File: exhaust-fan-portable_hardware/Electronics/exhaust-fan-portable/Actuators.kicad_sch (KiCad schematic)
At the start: 20 parts, among them Q1 NMOS, Q2 NMOS, Q3 NMOS, U3 LMV321, U6 LMV321, U7 LMV321

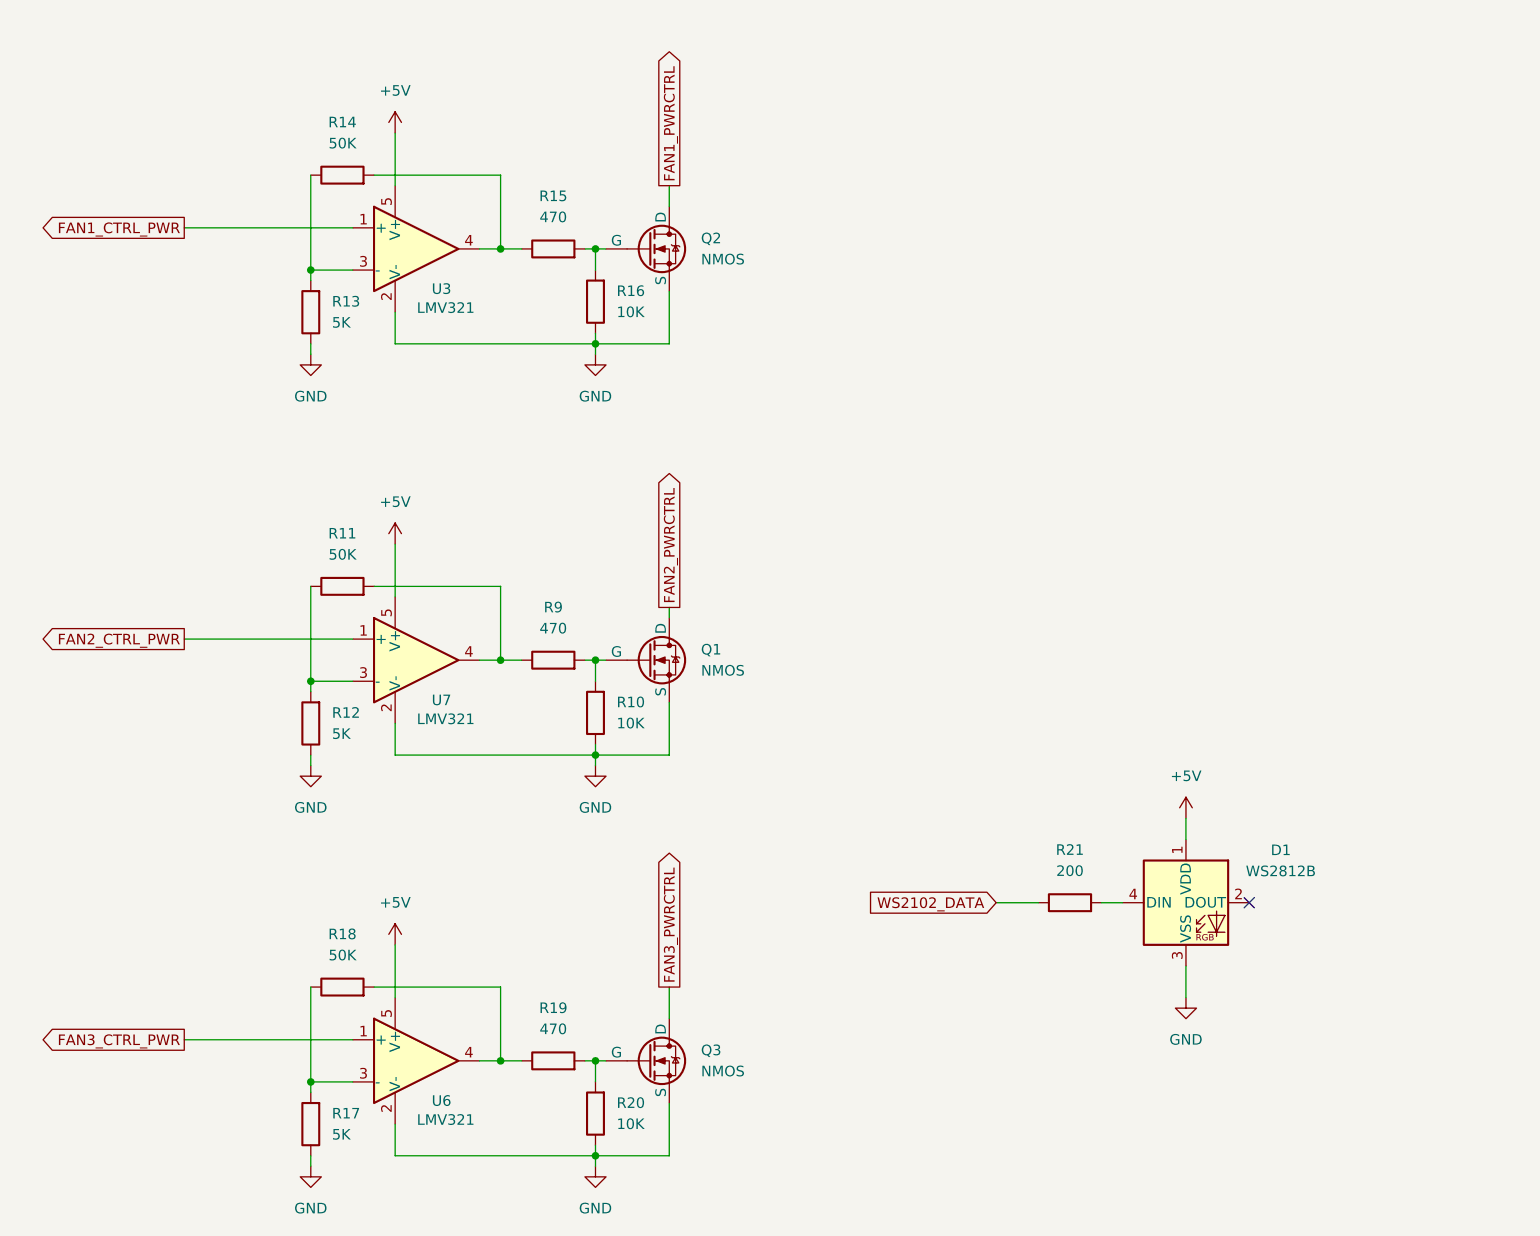
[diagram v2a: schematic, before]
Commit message: updated mechanical information
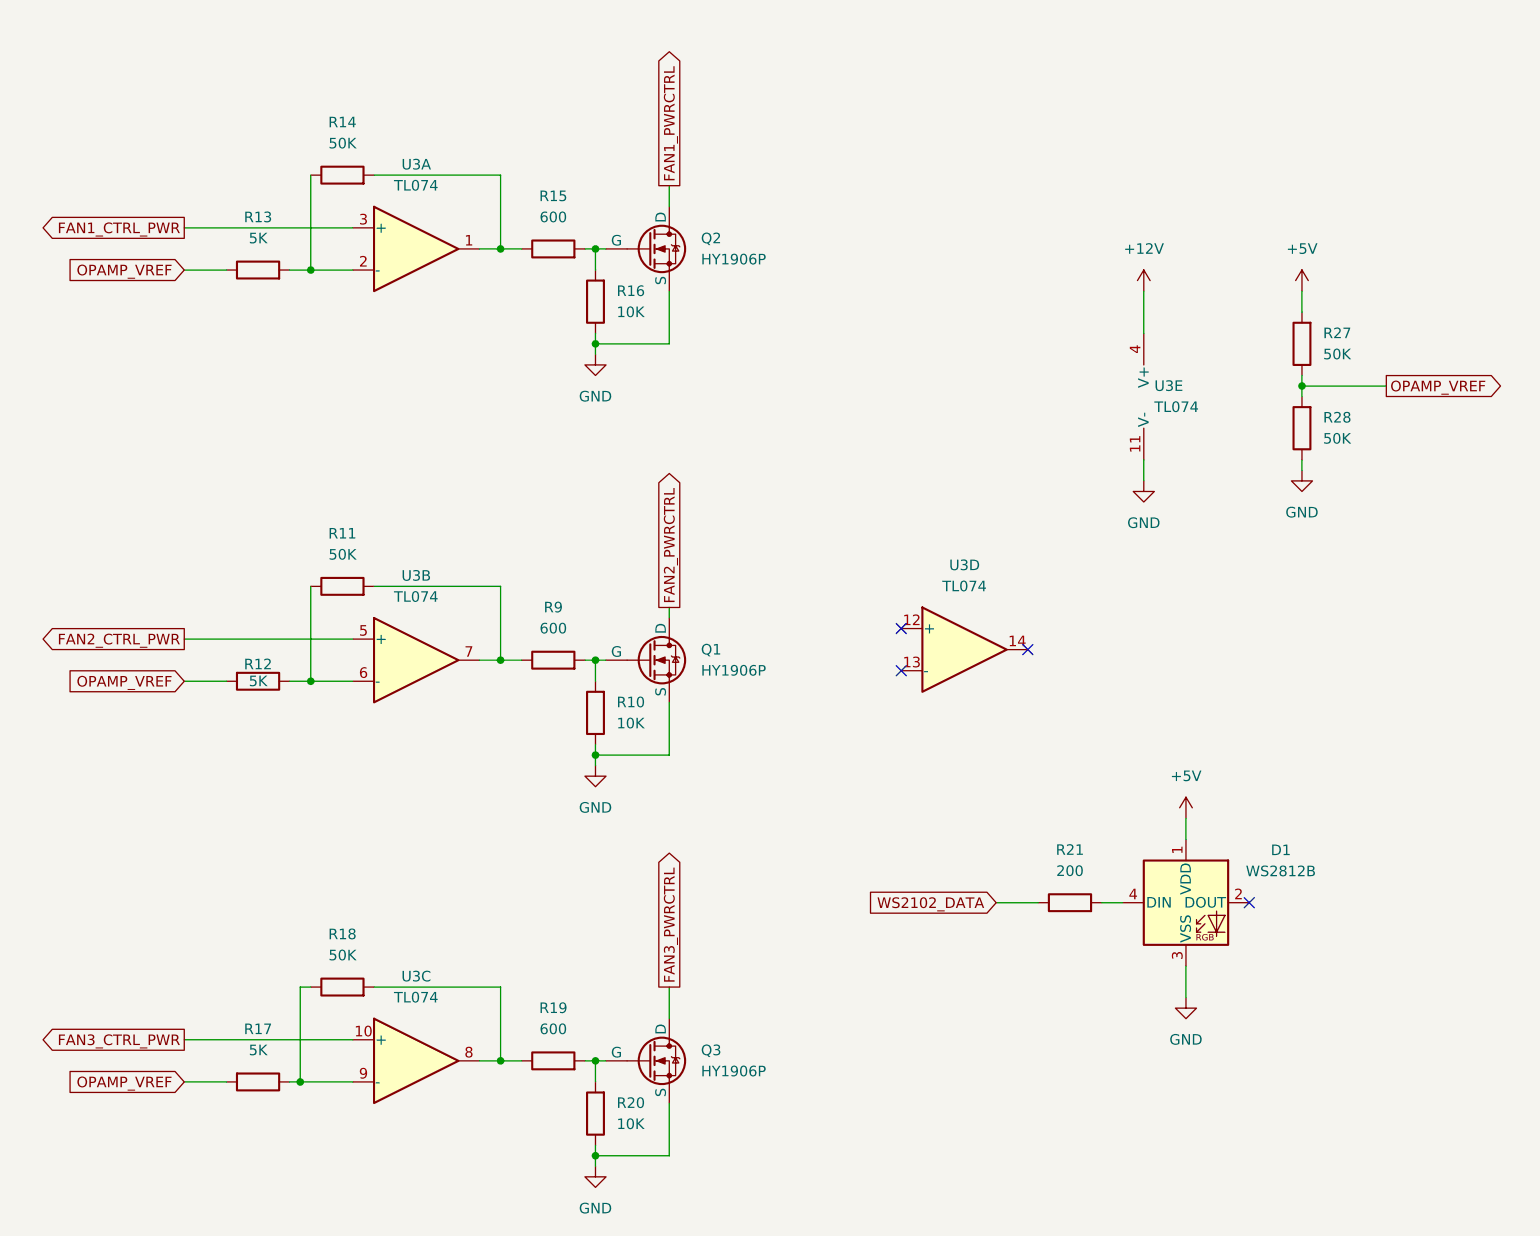
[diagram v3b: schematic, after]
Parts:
- removed U3, U6, U7: LMV321, Package_SO:SO-6_4.4x3.6mm_P1.27mm, symbol Amplifier_Operational:LMV321
- added R27, R28: 50K, Resistor_SMD:R_0603_1608Metric_Pad0.98x0.95mm_HandSolder, symbol Device:R
- added U3: TL074, Package_SO:SOIC-14_3.9x8.7mm_P1.27mm, symbol Amplifier_Operational:TL074
- Q1, Q2, Q3: value NMOS -> HY1906P
- R15, R19, R9: value 470 -> 600
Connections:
- net +5V: now also R27.2
- net FAN1_CTRL_PWR: now also U3.3 (+)
- net FAN2_CTRL_PWR: now also U3.5 (+)
- net FAN3_CTRL_PWR: now also U3.10 (+)
- net GND: now also R28.1, U3.11 (V-); no longer R12.1, R13.1, R17.1
- net at R11.1: now also R12.1, U3.6 (-); no longer R12.2
- net at R11.2, R9.1: now also U3.7
- net at R13.2, R14.1: now also U3.2 (-)
- net at R14.2, R15.1: now also U3.1
- net at R18.1: now also R17.1, U3.9 (-); no longer R17.2
- net at R18.2, R19.1: now also U3.8
- new net +12V: U3.4 (V+)
- new net OPAMP_VREF: R12.2, R13.1, R17.2, R27.1, R28.2
- no-connect marks 1 -> 4
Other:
- moved on the sheet: R12, R13, R17
